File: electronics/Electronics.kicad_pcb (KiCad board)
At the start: 4 copper layers, 133.1 x 97.5 mm, 80 parts, among them J1 3mm_pad, J10 215079-4, J11 215079-4, J12 215079-4, J13 3mm_pad, J14 3mm_pad, J15 FTSH-105-XX-X-DV, J16 10118193-0001LF, J2 3mm_pad, J3 3mm_pad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

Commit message: Relocated items
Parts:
- added C31: 4.7uF, Capacitor_SMD:C_1206_3216Metric_Pad1.33x1.80mm_HandSolder, F.Cu at (233.8, 108.7)
- C10, C13, C16, C19, C29: value 47uF -> 100uF; footprint Capacitor_THT:CP_Radial_D8.0mm_P3.50mm -> Capacitor_SMD:CP_Elec_8x10
- C2: footprint Capacitor_THT:CP_Radial_D5.0mm_P2.00mm -> Capacitor_SMD:C_1206_3216Metric_Pad1.33x1.80mm_HandSolder
- C25: value 4.7uF -> 470uF; footprint Capacitor_THT:CP_Radial_D5.0mm_P2.00mm -> Capacitor_THT:CP_Radial_D10.0mm_P5.00mm
- U1: value LQFP32_7X7_STM -> STM32G441KBT3
- moved R11 241.5 mm to (39.8, 177.6)
- moved R12 238.4 mm to (49.4, 178.6)
- moved C16 236.1 mm to (54.2, 150.6), turned to 0 degrees
- moved R13 224.7 mm to (64.2, 179.8)
- moved C17 212.5 mm to (59.4, 160.0)
- moved C18 203.5 mm to (66.6, 169.4)
- moved C13 198.8 mm to (107.8, 162.2), turned to 0 degrees
- moved R8 195.5 mm to (86.6, 175.0)
- moved R9 195.3 mm to (95.2, 178.6)
- moved C10 190.7 mm to (135.6, 173.8), turned to 0 degrees
- moved R10 189.9 mm to (111.4, 183.2)
- moved J5 178.3 mm to (77.6, 168.8)
- moved J6 178.1 mm to (78.2, 176.4)
- moved C14 159.6 mm to (113.8, 167.2)
- moved C15 155.2 mm to (117.9, 177.0)
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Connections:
- C10 pad 1: Vdrive -> GND
- C10 pad 2: GND -> Vdrive
- C13 pad 1: Vdrive -> GND
- C13 pad 2: GND -> Vdrive
- C16 pad 1: Vdrive -> GND
- C16 pad 2: GND -> Vdrive
- C2 pad 1: GND -> +3V3
- C2 pad 2: +3V3 -> GND
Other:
- board size 133.1 x 97.5 mm -> 102.4 x 75 mm

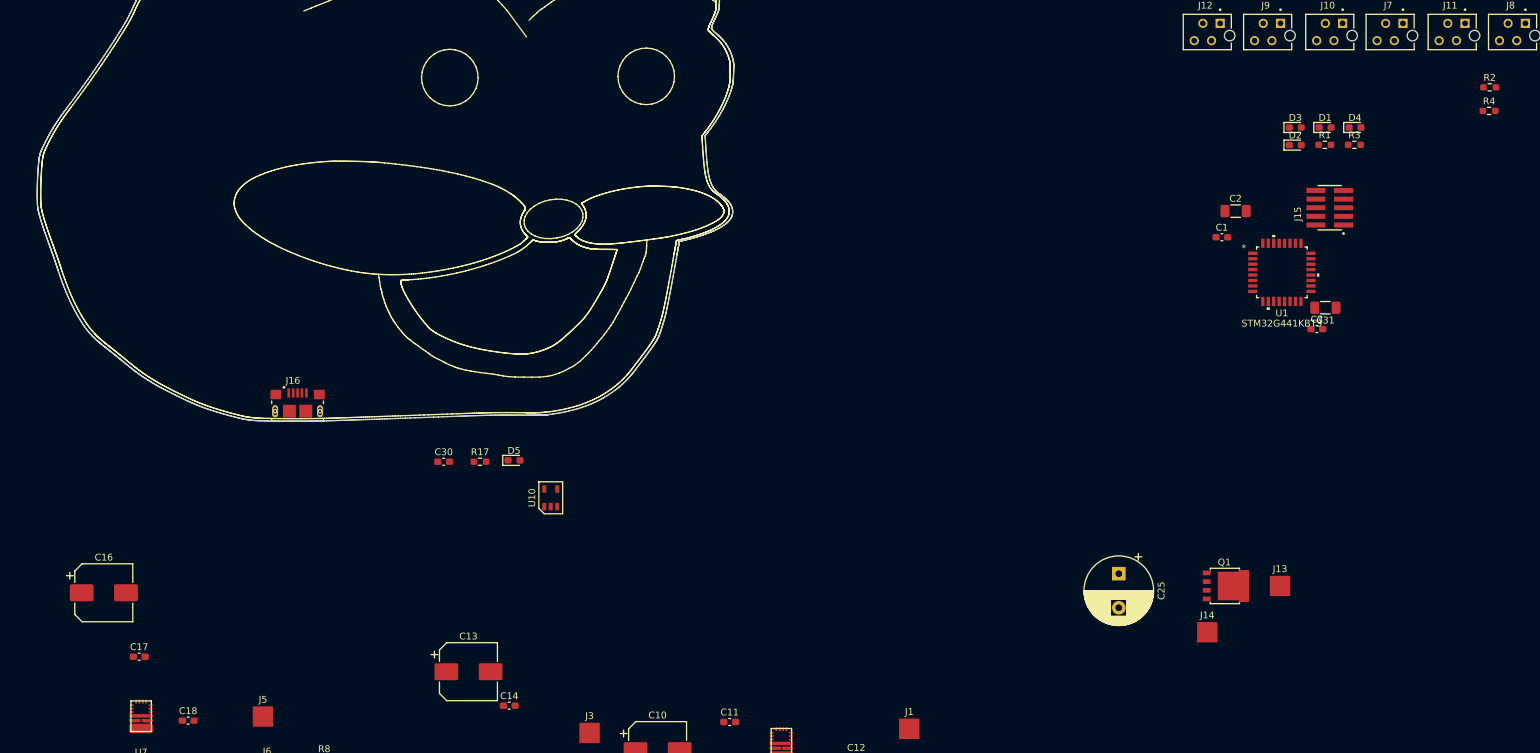
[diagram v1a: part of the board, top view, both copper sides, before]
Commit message: Moved usb
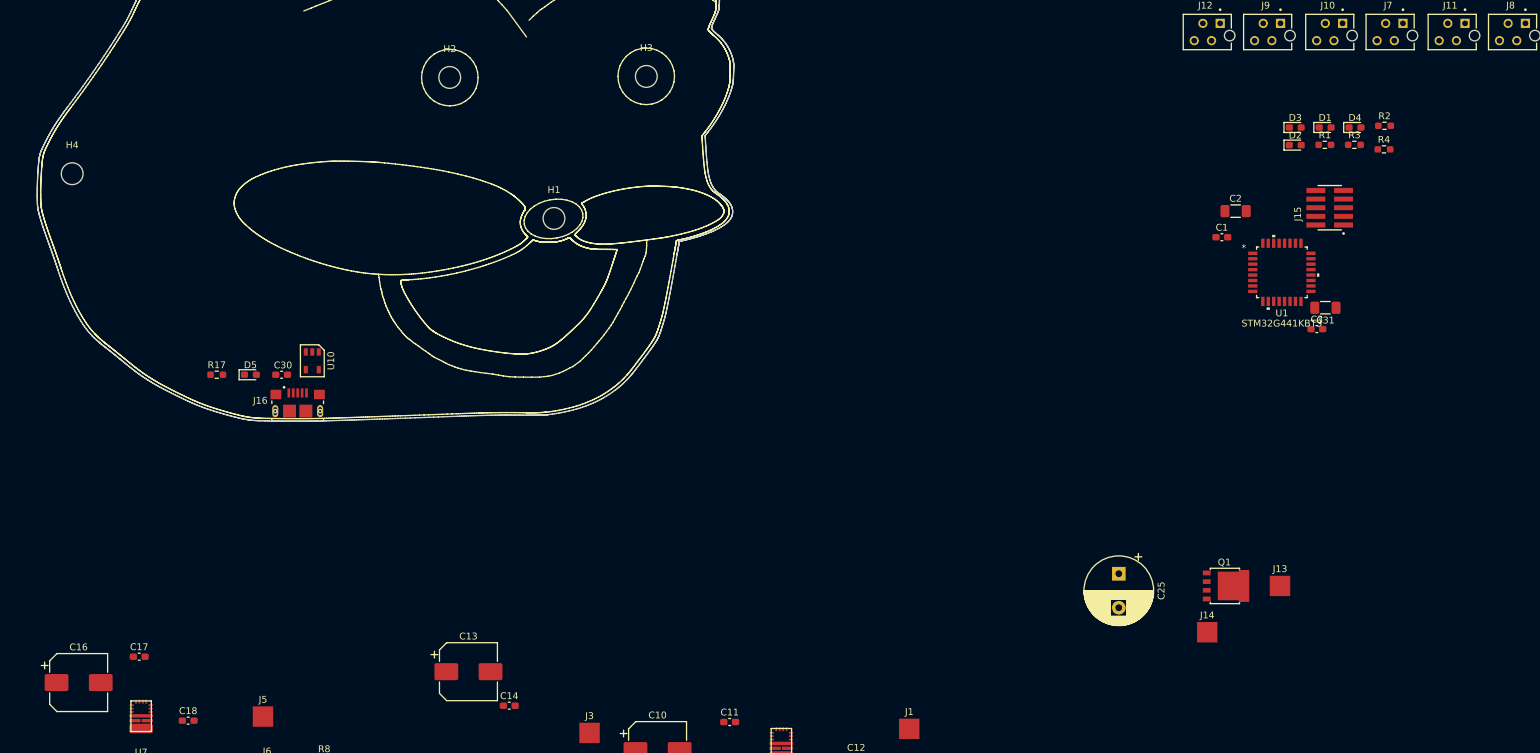
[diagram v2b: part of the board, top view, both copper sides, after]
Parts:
- added H1: MountingHole, MountingHole:MountingHole_3.2mm_M3, F.Cu at (120.4, 95.6)
- added H2: MountingHole, MountingHole:MountingHole_3.2mm_M3, F.Cu at (105.0, 74.8)
- added H3: MountingHole, MountingHole:MountingHole_3.2mm_M3, F.Cu at (133.9, 74.7)
- added H4: MountingHole, MountingHole:MountingHole_3.2mm_M3, F.Cu at (49.5, 89.0)
- moved R17 40.8 mm to (70.8, 118.5)
- moved D5 40.7 mm to (75.8, 118.5)
- moved U10 40.4 mm to (84.8, 116.5), turned to 180 degrees
- moved C30 27.0 mm to (80.3, 118.5)
- moved R2 16.5 mm to (242.5, 82.0)
- moved R4 16.5 mm to (242.4, 85.4)
- moved C16 13.7 mm to (50.5, 163.8)

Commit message: Sorting componenents on pcb
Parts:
- moved J13 170.1 mm to (62.7, 106.0), turned to 290 degrees
- moved R8 169.3 mm to (127.4, 10.7)
- moved C13 169.3 mm to (148.6, -2.07)
- moved C14 169.3 mm to (154.6, 2.93)
- moved R10 169.3 mm to (152.2, 18.9)
- moved R9 169.3 mm to (136.0, 14.3)
- moved J14 164.5 mm to (61.2, 102.0), turned to 290 degrees
- moved J7 157.9 mm to (87.3, 66.7), turned to 225 degrees
- moved Q1 156.7 mm to (68.3, 107.4), turned to 270 degrees
- moved U2 156.5 mm to (59.5, 56.0)
- moved C4 154.6 mm to (50.2, 53.0)
- moved C7 154.6 mm to (68.2, 53.2)
- moved U3 149.3 mm to (124.4, 148.3), turned to 180 degrees
- moved C5 143.9 mm to (118.3, 138.8)
- moved C8 143.9 mm to (134.4, 138.6)
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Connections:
- C10 pad 1: GND -> Earth
- C11 pad 1: GND -> Earth
- C13 pad 1: GND -> Earth
- C14 pad 1: GND -> Earth
- C16 pad 1: GND -> Earth
- C17 pad 1: GND -> Earth
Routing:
- net Vdrive: track 0.00 -> 96.2 mm
- net +5VL: track 0.00 -> 17.6 mm
- net Net-(C12-Pad2): track 0.00 -> 10.2 mm, vias 0 -> 2
- net Net-(C15-Pad2): track 0.00 -> 8.77 mm
- net Net-(C15-Pad1): track 0.00 -> 7.77 mm, vias 0 -> 2
- net Net-(C12-Pad1): track 0.00 -> 7.37 mm, vias 0 -> 2
- net /MCU-USB_DP: track 0.00 -> 4.84 mm
- net /MCU-USB_DM: track 0.00 -> 3.02 mm
- net Net-(D5-Pad1): track 0.00 -> 1.91 mm
- net +3V3: track 0.00 -> 1.77 mm
- net Net-(R5-Pad2): track 0.00 -> 1.62 mm
- net Net-(R6-Pad2): track 0.00 -> 1.58 mm
- net Net-(R7-Pad2): track 0.00 -> 1.57 mm
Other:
- board text added: "BOTTOM TEXT"
- board text added: "MIDDLE TEXT"
- board text added: "TOP TEXT"

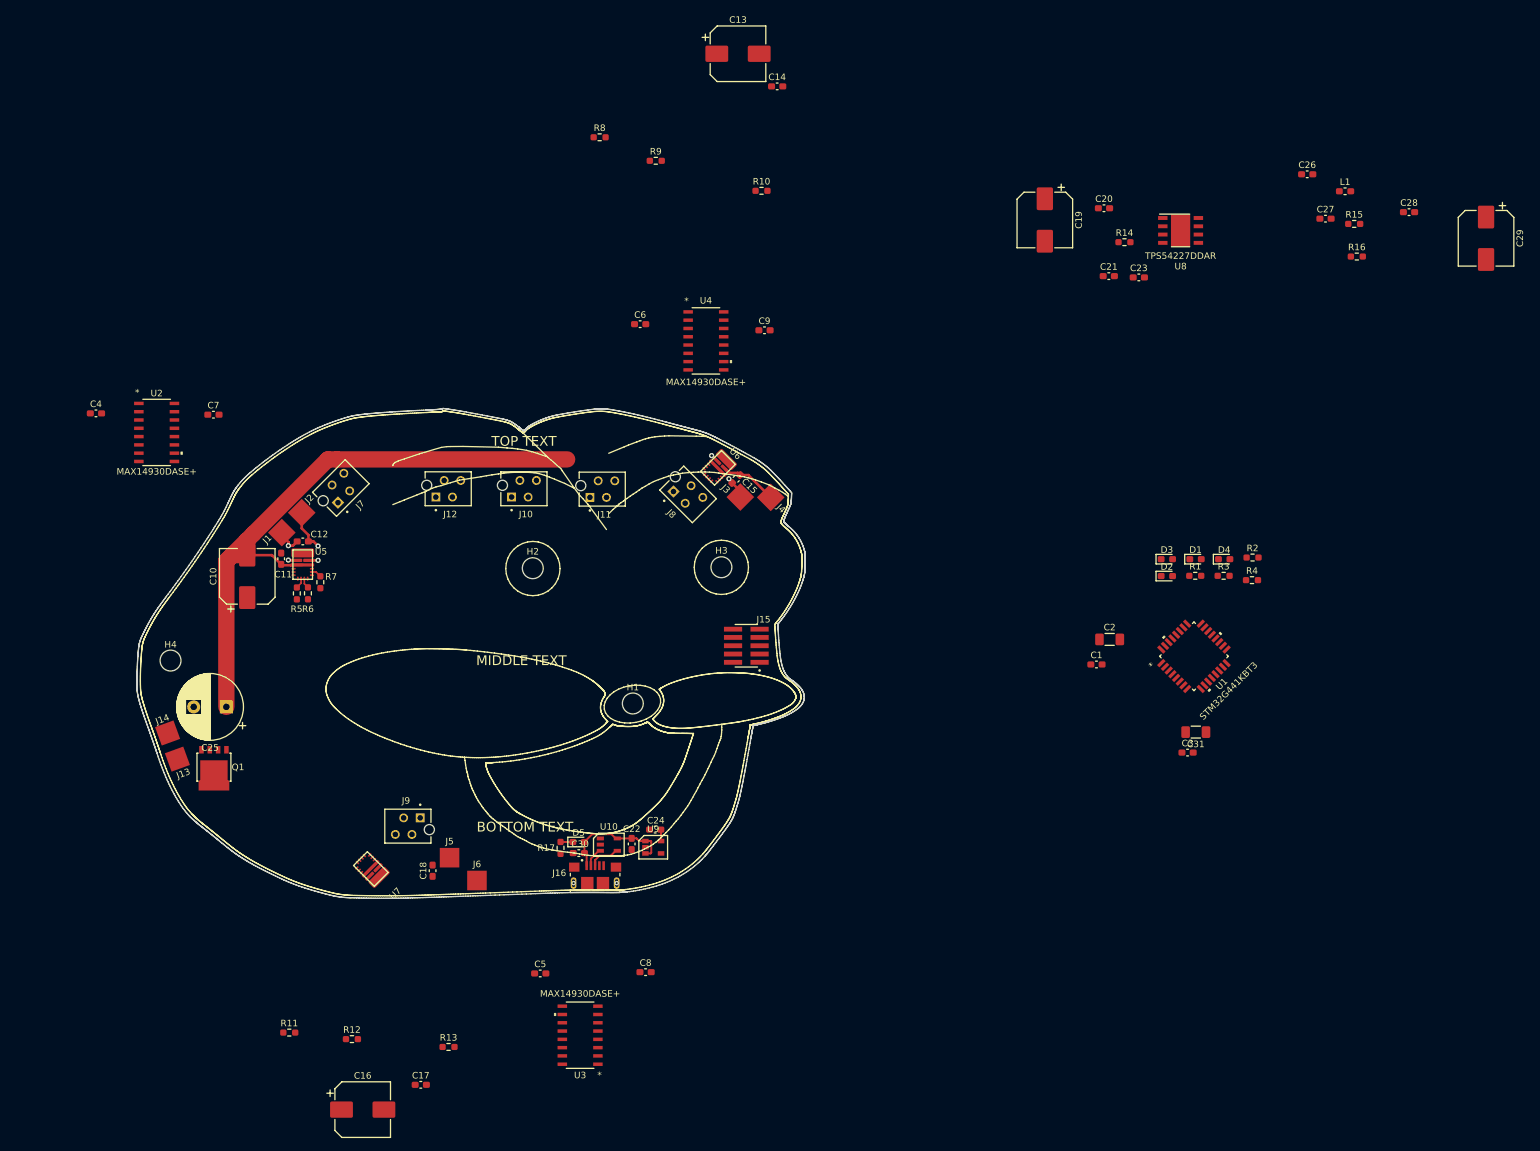
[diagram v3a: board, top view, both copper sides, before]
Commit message: Fixed motor connectors, added vbat to 5v
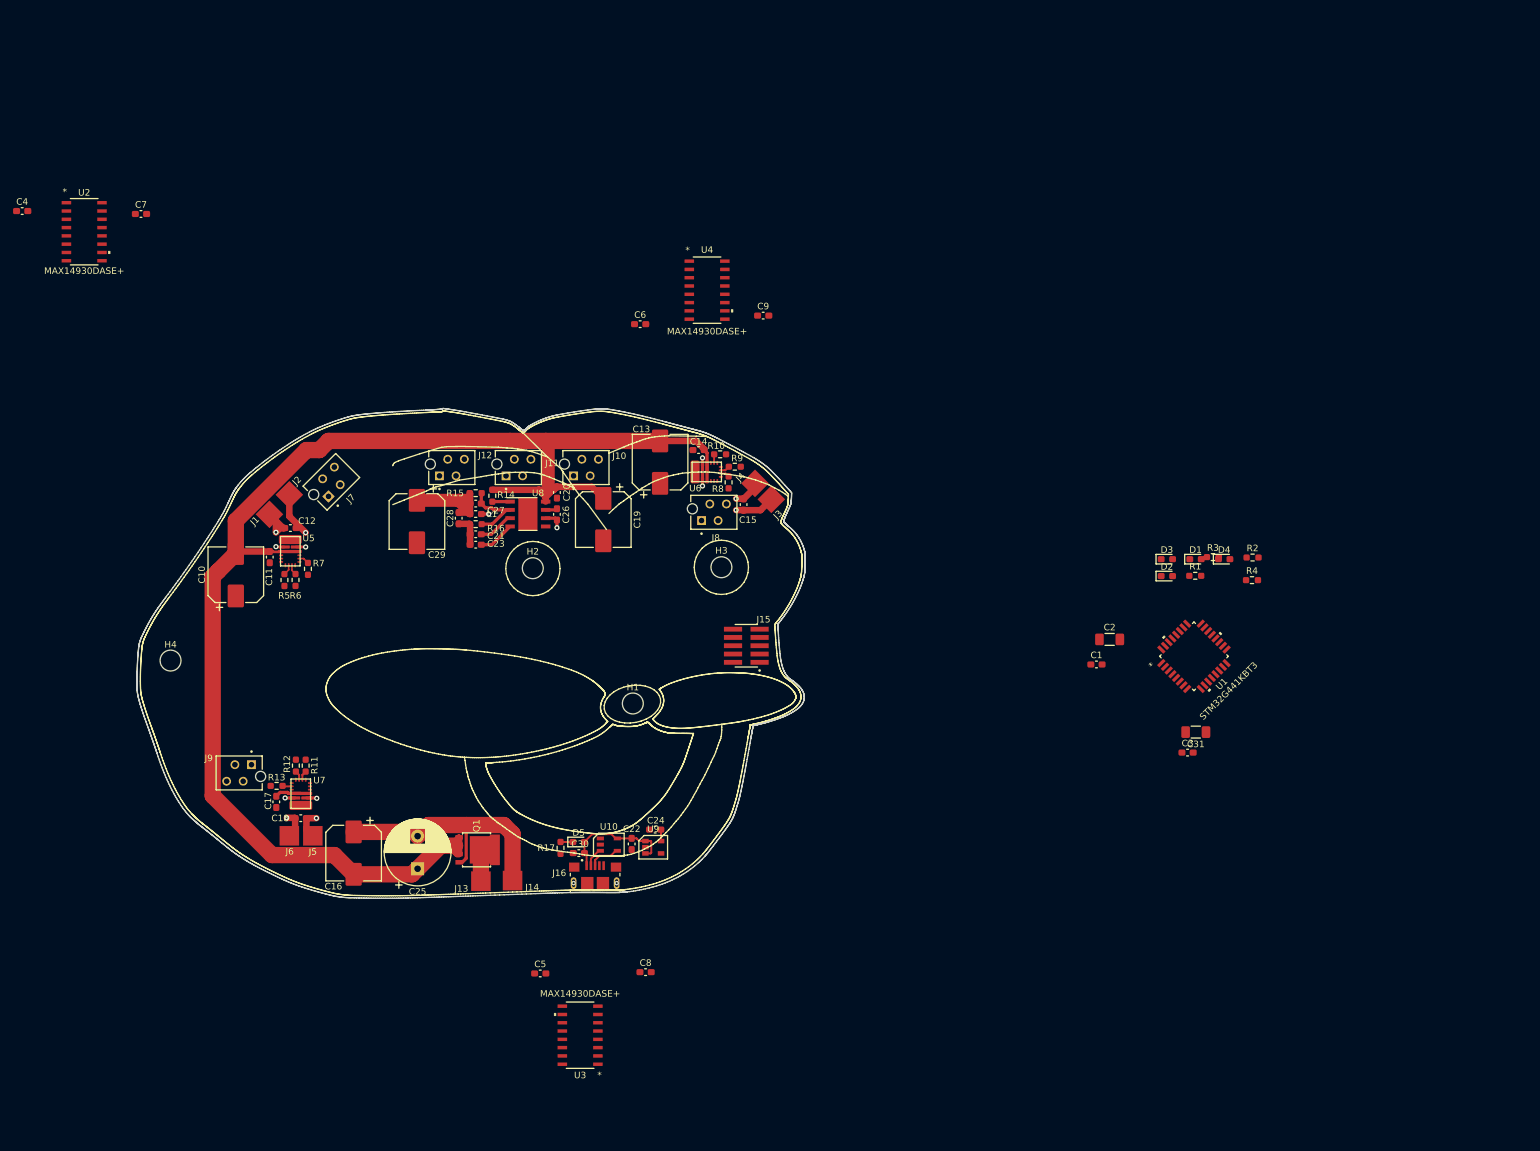
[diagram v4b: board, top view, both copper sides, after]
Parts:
- moved C29 169.5 mm to (99.4, 69.6)
- moved C28 153.0 mm to (105.8, 69.1), turned to 90 degrees
- moved L1 142.1 mm to (108.4, 68.5), turned to 180 degrees
- moved R16 141.1 mm to (108.4, 70.0), turned to 180 degrees
- moved R15 140.8 mm to (108.4, 65.2)
- moved C27 137.3 mm to (108.4, 66.8), turned to 180 degrees
- moved C26 126.2 mm to (120.8, 68.5), turned to 270 degrees
- moved C23 109.5 mm to (108.4, 73.2)
- moved U8 109.0 mm to (116.4, 68.5)
- moved C21 104.8 mm to (108.4, 71.5)
- moved R14 104.4 mm to (111.0, 65.7), turned to 270 degrees
- moved C20 94.5 mm to (120.8, 65.2), turned to 90 degrees
- moved C19 81.8 mm to (128.0, 69.3)
- moved C13 63.7 mm to (136.7, 60.5), turned to 90 degrees
- moved J14 57.5 mm to (114.0, 124.6), turned to 270 degrees
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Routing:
- net Vdrive: track 96.2 -> 218.1 mm
- net Earth: track 0.00 -> 46.2 mm
- net Net-(C26-Pad2): track 0.00 -> 15.5 mm, vias 0 -> 2
- net +5VD: track 0.00 -> 14.1 mm
- net Net-(C27-Pad1): track 0.00 -> 11.7 mm
- net Net-(C18-Pad1): track 0.00 -> 9.28 mm, vias 0 -> 2
- net Net-(C18-Pad2): track 0.00 -> 9.02 mm, vias 0 -> 2
- net Net-(C23-Pad2): track 0.00 -> 5.57 mm
- net Net-(C21-Pad2): track 0.00 -> 5.43 mm
- net Net-(J13-Pad1): track 0.00 -> 4.83 mm
- net Net-(C12-Pad1): track 7.37 -> 11.5 mm
- net Net-(C15-Pad2): track 8.77 -> 5.52 mm, vias 0 -> 2
- net Net-(R14-Pad2): track 0.00 -> 2.73 mm
- net Net-(C26-Pad1): track 0.00 -> 1.80 mm
- net Net-(R9-Pad2): track 0.00 -> 1.47 mm
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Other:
- board text removed: "BOTTOM TEXT"
- board text removed: "MIDDLE TEXT"
- board text removed: "TOP TEXT"

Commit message: Great success
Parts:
- U1: value STM32G441KBT3 -> STM32G441KB
- moved C31 106.1 mm to (113.5, 88.0)
- moved C4 105.9 mm to (124.2, 84.8), turned to 180 degrees
- moved U1 103.9 mm to (114.7, 95.2), turned to 135 degrees
- moved C3 101.1 mm to (117.7, 88.4), turned to 180 degrees
- moved U2 97.1 mm to (128.4, 80.3), turned to 90 degrees
- moved D4 96.7 mm to (130.6, 103.6), turned to 180 degrees
- moved R4 96.5 mm to (134.1, 103.6), turned to 180 degrees
- moved R2 94.2 mm to (134.2, 88.6), turned to 180 degrees
- moved R3 92.7 mm to (134.1, 106.5), turned to 180 degrees
- moved C2 92.2 mm to (114.7, 103.4), turned to 180 degrees
- moved C1 89.8 mm to (114.8, 105.4), turned to 180 degrees
- moved D1 89.5 mm to (130.7, 91.6), turned to 180 degrees
- moved D3 89.3 mm to (130.6, 106.5), turned to 180 degrees
- moved C7 85.7 mm to (124.2, 75.8)
- moved R1 85.5 mm to (134.2, 91.6), turned to 180 degrees
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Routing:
- net Earth: track 46.2 -> 257.3 mm, vias 0 -> 1
- net +3V3: track 1.77 -> 204.2 mm, vias 0 -> 4
- net /Driver/MOT_sleep: track 0.00 -> 145.2 mm, vias 0 -> 7
- net /Driver/MOT_off: track 0.00 -> 133.5 mm, vias 0 -> 6
- net +5VD: track 14.1 -> 120.1 mm, vias 0 -> 4
- net GND: track 0.00 -> 90.9 mm, vias 0 -> 12
- net /Driver/MOT1en_2: track 0.00 -> 55.4 mm, vias 0 -> 2
- net /Driver/MOT1en_1: track 0.00 -> 52.1 mm, vias 0 -> 2
- net /TRW_PWM: track 0.00 -> 36.5 mm, vias 0 -> 1
- net /Aim-serv_PWM: track 0.00 -> 24.3 mm, vias 0 -> 1
- net /Driver/MOT2en_1: track 0.00 -> 23.7 mm, vias 0 -> 2
- net /Driver/MOT2en_2: track 0.00 -> 23.2 mm, vias 0 -> 2
- net /Hold-serv_PWM: track 0.00 -> 20.9 mm, vias 0 -> 1
- net Net-(C15-Pad2): track 5.52 -> 19.0 mm
- net /Driver/MOT3en_2: track 0.00 -> 8.29 mm, vias 0 -> 2
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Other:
- net class Default: clearance 0.2 -> 0.127
- rule trace_clearance: 0.2 -> 0.127
